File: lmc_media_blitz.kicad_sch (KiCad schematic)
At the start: 46 parts, among them J1 Conn_ARM_JTAG_SWD_10, Q1 BSS138, Q2 BSS138, U1 TPS61222DCK, U2 TLV77333PDBVR, U3 LPC804M101JDH20, U4 ST25R3918AQW, U5 SK9822, U6 SK9822, U7 SK9822, U8 SK9822, U9 SK9822, Y1 27.12MHz

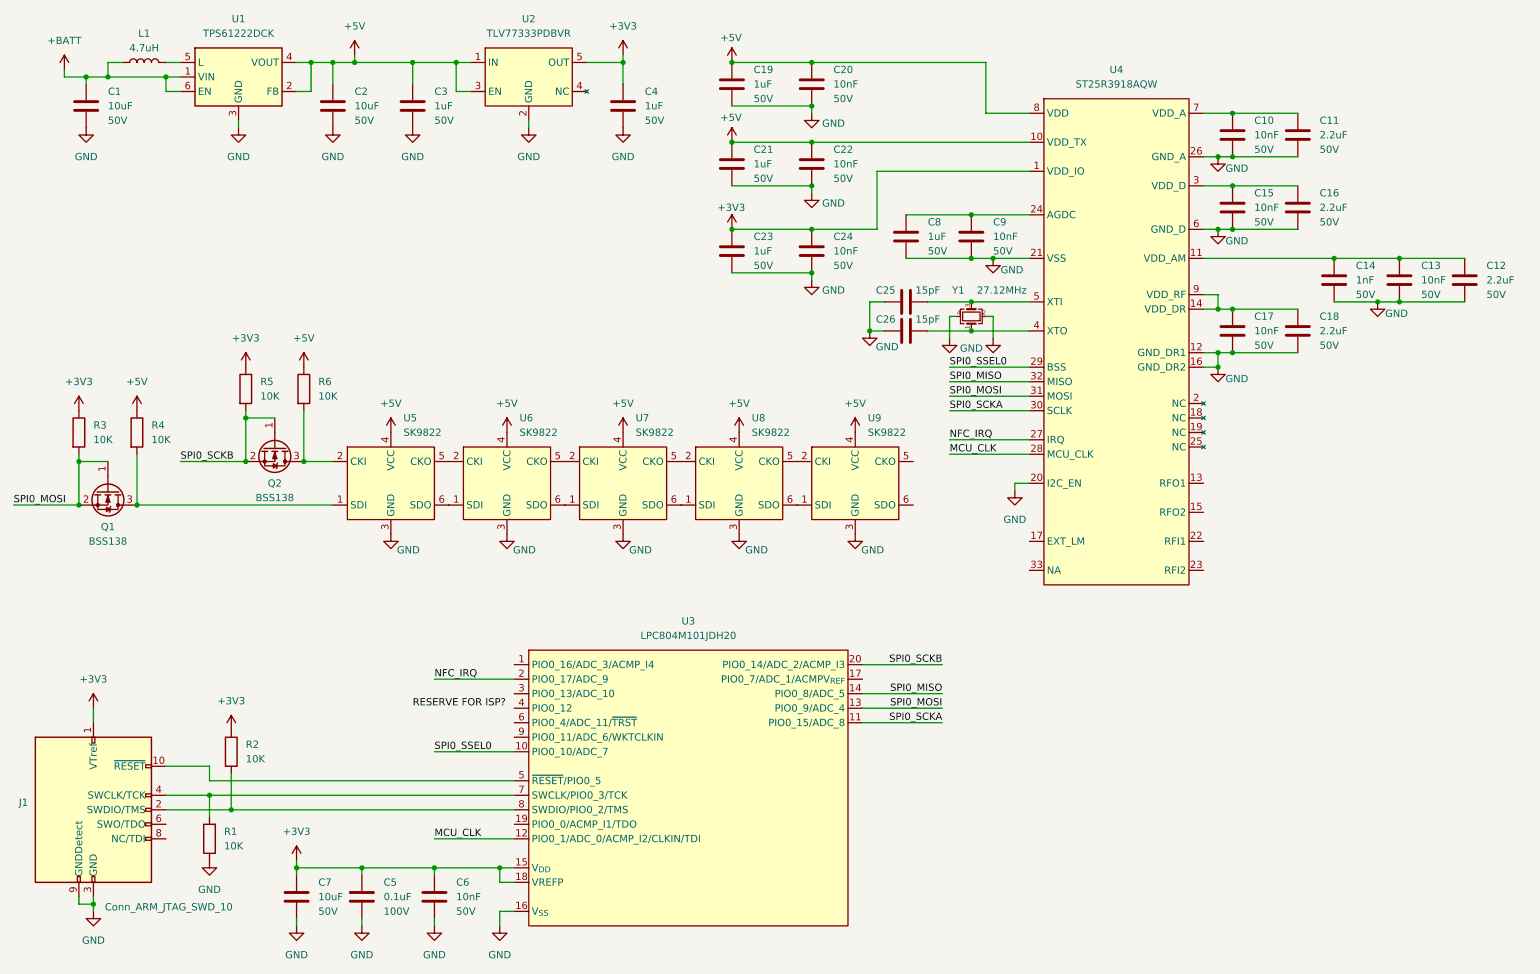
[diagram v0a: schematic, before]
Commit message: Added some footprints and cap touch symbols
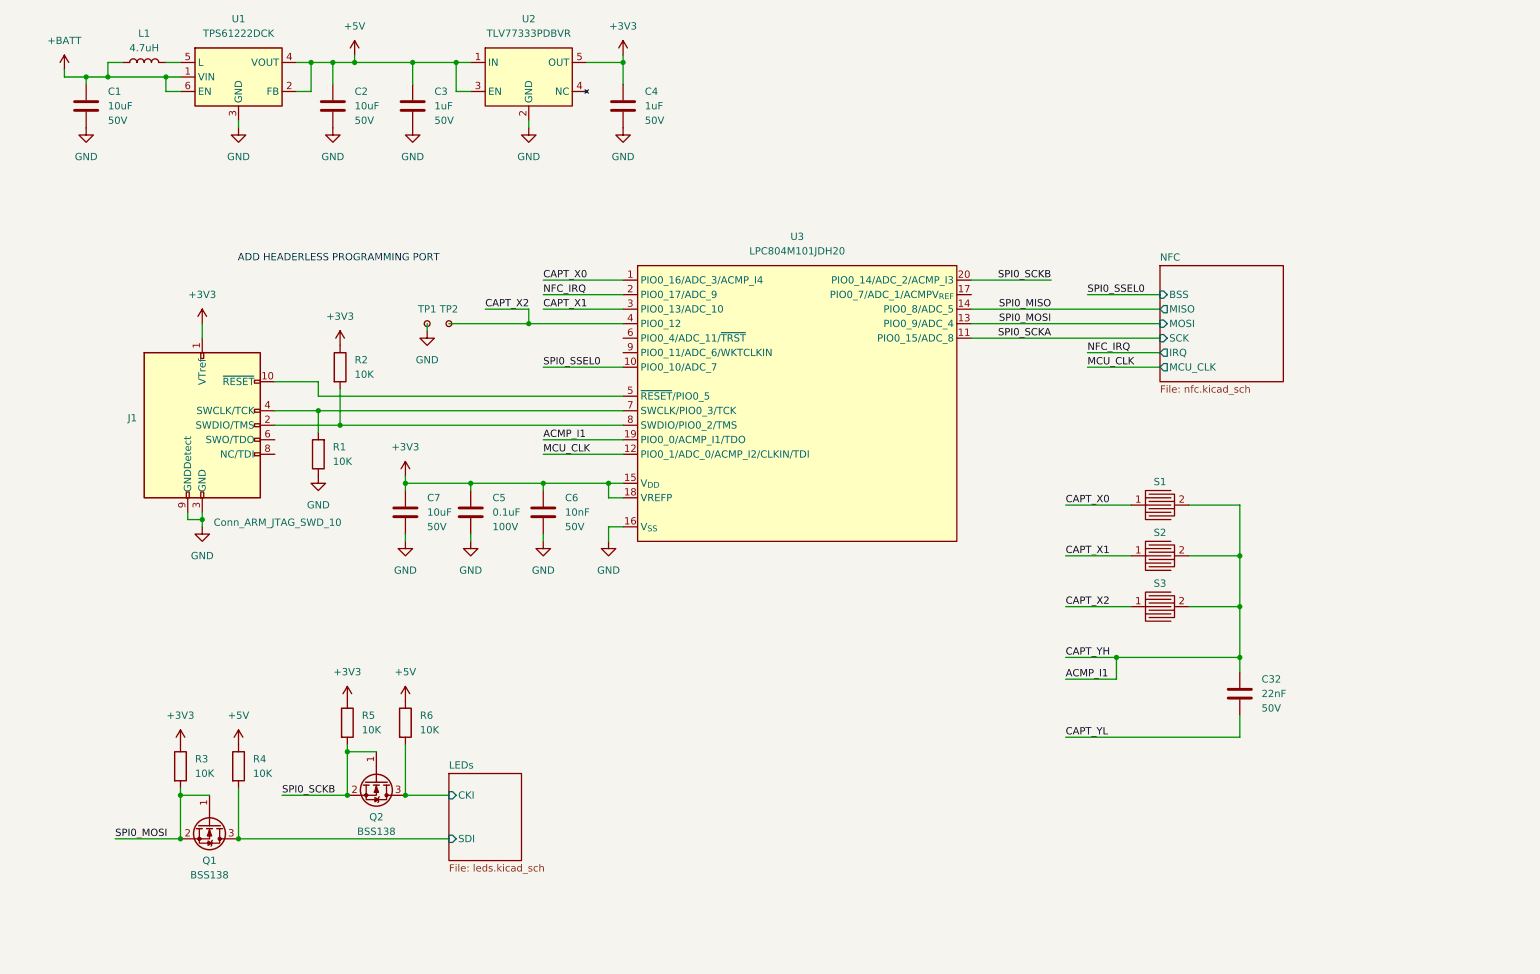
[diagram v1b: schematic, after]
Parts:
- removed C10, C13, C15, C17, C20, C22, C24, C9: 10nF, 0805, symbol Device:C
- removed C11, C12, C16, C18: 2.2uF, 0805, symbol Device:C
- removed C14: 1nF, 0805, symbol Device:C
- removed C19, C21, C23, C8: 1uF, 0805, symbol Device:C
- removed C25, C26: 15pF, 0603, symbol Device:C
- removed U4: ST25R3918AQW, VFQFPN32, symbol parts:ST25R3918AQW
- removed U5, U6, U7, U8, U9: SK9822, symbol parts:SK99822
- removed Y1: 27.12MHz, SMD3225-4P, symbol Device:Crystal_GND24_Small
- added C32: 22nF, 0805, symbol Device:C
- added S1, S2, S3: ~, symbol parts:CapTouchPad
- added TP1, TP2: TestPoint_Small, symbol Connector:TestPoint_Small
- C1, C2, C3, C4, C5, C6, C7: footprint 0805 -> Capacitor_SMD:C_0805_2012Metric
- J1: MFPN (none) -> FTSH-105-01-L-DV-007-K
- L1: footprint (none) -> Inductor_SMD:L_Taiyo-Yuden_MD-3030
- R1, R2, R3, R4, R5, R6: footprint 0805 -> Resistor_SMD:R_0805_2012Metric
- U2: footprint SOT23-5 -> Package_TO_SOT_SMD:SOT-23-5
- U3: footprint SOT360-1 -> Package_SO:TSSOP-20_4.4x6.5mm_P0.65mm
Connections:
- net GND: now also TP1.1
- net LEDs/SDI: now reaches Q1.3 (D), R4.2
- net LEDs/CKI: now reaches Q2.3 (D), R6.2
- net CAPT_X0: now reaches U3.1 (PIO0_16/ADC_3/ACMP_I4)
- net CAPT_X0: now also S1.1
- net ACMP_I1: now reaches U3.19 (PIO0_0/ACMP_I1/TDO)
- net ACMP_I1: now also C32.1, S1.2, S2.2, S3.2
- net CAPT_X1: now reaches U3.3 (PIO0_13/ADC_10)
- net CAPT_X1: now also S2.1
- net CAPT_X2: now reaches U3.4 (PIO0_12)
- net CAPT_X2: now also S3.1, TP2.1
- new net CAPT_YL: C32.2
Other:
- added sheet LEDs (leds.kicad_sch)
- added sheet NFC (nfc.kicad_sch)
- note added: "ADD HEADERLESS PROGRAMMING PORT"
- moved on the sheet: C5, C6, C7, J1, Q1, Q2, R1, R2, R3, R4, R5, R6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

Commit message: Adding some stuf
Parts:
- added J2, J3: ~, footprints:Keystone82, symbol parts:Keystone82
- C32: footprint 0805 -> Capacitor_SMD:C_0805_2012Metric
- J1: footprint (none) -> Capacitor_SMD:C_0805_2012Metric
- TP1, TP2: footprint (none) -> TestPoint:TestPoint_Pad_D2.0mm
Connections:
- net +BATT: now also J2.1, J2.2
- net ACMP_I1: now also U3.9 (PIO0_11/ADC_6/WKTCLKIN)
- net CAPT_YL: now also U3.6 (PIO0_4/ADC_11/~{TRST})
- net GND: now also J3.1, J3.2
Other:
- moved on the sheet: C1, C2, C3, C32, C4, C5, C6, C7, J1, L1, Q1, Q2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

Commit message: WIP
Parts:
- added TP3, TP4: TestPoint_Small, TestPoint:TestPoint_Pad_D2.0mm, symbol Connector:TestPoint_Small
- C5: footprint Capacitor_SMD:C_0805_2012Metric -> Capacitor_SMD:C_0603_1608Metric; MFPN CL21B104KCFNNNE -> CC0603KRX7R9BB104; Voltage 100V -> 50V
- C6: footprint Capacitor_SMD:C_0805_2012Metric -> Capacitor_SMD:C_0603_1608Metric; MFPN CL21B103KBANNNC -> CC0603KRX7R9BB103
- renumbered J2 to J1, J3 to J2, J1 to J3
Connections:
- net +3V3: now also TP4.1
- net +5V: now also TP3.1
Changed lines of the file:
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@@
 	)
 	(junction
+		(at 125.73 27.94)
+		(diameter 0)
+		(color 0 0 0 0)
+	)
+	(junction
 		(at 226.06 140.97)
 		(diameter 0)
@@
 	)
 	(junction
+		(at 88.9 27.94)
+		(diameter 0)
+		(color 0 0 0 0)
+	)
+	(junction
 		(at 204.47 140.97)
 		(diameter 0)
@@
 	(wire
 		(pts
-			(xy 124.46 27.94) (xy 130.81 27.94)
+			(xy 124.46 27.94) (xy 125.73 27.94)
 		)
 		(stroke
@@
 	(wire
 		(pts
+			(xy 88.9 25.4) (xy 88.9 27.94)
+		)
+		(stroke
+			(width 0)
+			(type default)
+		)
+	)
+	(wire
+		(pts
 			(xy 115.57 113.03) (xy 115.57 110.49)
 		)
@@
 	(wire
 		(pts
+			(xy 88.9 27.94) (xy 93.98 27.94)
+		)
+		(stroke
+			(width 0)
+			(type default)
+		)
+	)
+	(wire
+		(pts
 			(xy 199.39 87.63) (xy 212.09 87.63)
 		)
@@
 	(wire
 		(pts
+			(xy 125.73 27.94) (xy 130.81 27.94)
+		)
+		(stroke
+			(width 0)
+			(type default)
+		)
+	)
+	(wire
+		(pts
 			(xy 33.02 30.48) (xy 33.02 29.21)
 		)
@@
 	(wire
 		(pts
+			(xy 125.73 25.4) (xy 125.73 27.94)
+		)
+		(stroke
+			(width 0)
+			(type default)
+		)
+	)
+	(wire
+		(pts
 			(xy 195.58 144.78) (xy 204.47 144.78)
 		)
@@
 	(wire
 		(pts
-			(xy 83.82 27.94) (xy 93.98 27.94)
+			(xy 83.82 27.94) (xy 88.9 27.94)
 		)
 		(stroke
@@
 		(on_board yes)
 		(dnp no)
-		(property "Reference" "J3"
+		(property "Reference" "J2"
 			(at 22.606 49.53 0)
 			(effects
@@
 			(project "lmc_media_blitz"
 				(path "/b87eb037-3127-4116-a225-5eb939725614"
-					(reference "J3")
+					(reference "J2")
 					(unit 1)
 				)
@@
 	)
 	(symbol
+		(lib_id "Connector:TestPoint_Small")
+		(at 88.9 25.4 90)
+		(unit 1)
+		(exclude_from_sim no)
+		(in_bom yes)
+		(on_board yes)
+		(dnp no)
+		(fields_autoplaced yes)
+		(property "Reference" "TP3"
+			(at 88.9 22.86 90)
+			(effects
+				(font
+					(size 1.27 1.27)
+				)
+			)
+		)
+		(property "Value" "TestPoint_Small"
+			(at 90.1699 24.13 0)
+			(effects
+				(font
+					(size 1.27 1.27)
+				)
+				(justify left)
+				(hide yes)
+			)
+		)
+		(property "Footprint" "TestPoint:TestPoint_Pad_D2.0mm"
+			(at 88.9 20.32 0)
+			(effects
+				(font
+					(size 1.27 1.27)
+				)
+				(hide yes)
+			)
+		)
+		(property "Datasheet" "~"
+			(at 88.9 20.32 0)
+			(effects
+				(font
+					(size 1.27 1.27)
+				)
+				(hide yes)
+			)
+		)
+		(property "Description" "test point"
+			(at 88.9 25.4 0)
+			(effects
+				(font
+					(size 1.27 1.27)
+				)
+				(hide yes)
+			)
+		)
+		(pin "1"
+		)
+		(instances
+			(project "lmc_media_blitz"
+				(path "/b87eb037-3127-4116-a225-5eb939725614"
+					(reference "TP3")
+					(unit 1)
+				)
+			)
+		)
+	)
+	(symbol
 		(lib_id "Device:C")
 		(at 36.83 35.56 180)
@@
 		(on_board yes)
 		(dnp no)
-		(property "Reference" "J1"
+		(property "Reference" "J3"
 			(at 33.02 99.0599 0)
 			(effects
@@
 			(project ""
 				(path "/b87eb037-3127-4116-a225-5eb939725614"
-					(reference "J1")
+					(reference "J3")
 					(unit 1)
 				)
@@
 		(dnp no)
 		(fields_autoplaced yes)
-		(property "Reference" "J2"
+		(property "Reference" "J1"
 			(at 22.606 21.59 0)
 			(effects
@@
 			(project ""
 				(path "/b87eb037-3127-4116-a225-5eb939725614"
-					(reference "J2")
+					(reference "J1")
 					(unit 1)
 				)
@@
 	)
 	(symbol
+		(lib_id "Device:C")
+		(at 104.14 115.57 0)
+		(unit 1)
+		(exclude_from_sim no)
+		(in_bom yes)
+		(on_board yes)
+		(dnp no)
+		(fields_autoplaced yes)
+		(property "Reference" "C6"
+			(at 107.95 113.0299 0)
+			(effects
+				(font
+					(size 1.27 1.27)
+				)
+				(justify left)
+			)
+		)
+		(property "Value" "10nF"
+			(at 107.95 115.5699 0)
+			(effects
+				(font
+					(size 1.27 1.27)
+				)
+				(justify left)
+			)
+		)
+		(property "Footprint" "Capacitor_SMD:C_0603_1608Metric"
+			(at 105.1052 119.38 0)
+			(effects
+				(font
+					(size 1.27 1.27)
+				)
+				(hide yes)
+			)
+		)
+		(property "Datasheet" "~"
+			(at 104.14 115.57 0)
+			(effects
+				(font
+					(size 1.27 1.27)
+				)
+				(hide yes)
+			)
+		)
+		(property "Description" "Unpolarized capacitor"
+			(at 104.14 115.57 0)
+			(effects
+				(font
+					(size 1.27 1.27)
+				)
+				(hide yes)
+			)
+		)
+		(property "MFPN" "CC0603KRX7R9BB103"
+			(at 104.14 115.57 0)
+			(effects
+				(font
+					(size 1.27 1.27)
+				)
+				(hide yes)
+			)
+		)
+		(property "Voltage" "50V"
+			(at 107.95 118.1099 0)
+			(effects
+				(font
+					(size 1.27 1.27)
+				)
+				(justify left)
+			)
+		)
+		(pin "1"
+		)
+		(pin "2"
+		)
+		(instances
+			(project "lmc_media_blitz"
+				(path "/b87eb037-3127-4116-a225-5eb939725614"
+					(reference "C6")
+					(unit 1)
+				)
+			)
+		)
+	)
+	(symbol
 		(lib_id "power:+BATT")
 		(at 33.02 29.21 0)
@@
 			)
 		)
-		(property "Footprint" "Capacitor_SMD:C_0805_2012Metric"
+		(property "Footprint" "Capacitor_SMD:C_0603_1608Metric"
 			(at 92.4052 119.38 0)
 			(effects
@@
 			)
 		)
-		(property "MFPN" "CL21B104KCFNNNE"
+		(property "MFPN" "CC0603KRX7R9BB104"
 			(at 91.44 115.57 0)
 			(effects
@@
 			)
 		)
-		(property "Voltage" "100V"
+		(property "Voltage" "50V"
 			(at 95.25 118.1099 0)
 			(effects
@@
 	)
 	(symbol
-		(lib_id "Device:C")
-		(at 104.14 115.57 0)
-		(unit 1)
-		(exclude_from_sim no)
-		(in_bom yes)
-		(on_board yes)
-		(dnp no)
-		(fields_autoplaced yes)
-		(property "Reference" "C6"
-			(at 107.95 113.0299 0)
-			(effects
-				(font
-					(size 1.27 1.27)
-				)
-				(justify left)
-			)
-		)
-		(property "Value" "10nF"
-			(at 107.95 115.5699 0)
-			(effects
-				(font
-					(size 1.27 1.27)
-				)
-				(justify left)
-			)
-		)
-		(property "Footprint" "Capacitor_SMD:C_0805_2012Metric"
-			(at 105.1052 119.38 0)
-			(effects
-				(font
-					(size 1.27 1.27)
-				)
-				(hide yes)
-			)
-		)
-		(property "Datasheet" "~"
-			(at 104.14 115.57 0)
-			(effects
-				(font
-					(size 1.27 1.27)
-				)
-				(hide yes)
-			)
-		)
-		(property "Description" "Unpolarized capacitor"
-			(at 104.14 115.57 0)
-			(effects
-				(font
-					(size 1.27 1.27)
-				)
-				(hide yes)
-			)
-		)
-		(property "MFPN" "CL21B103KBANNNC"
-			(at 104.14 115.57 0)
-			(effects
-				(font
-					(size 1.27 1.27)
-				)
-				(hide yes)
-			)
-		)
-		(property "Voltage" "50V"
-			(at 107.95 118.1099 0)
-			(effects
-				(font
-					(size 1.27 1.27)
-				)
-				(justify left)
-			)
-		)
-		(pin "1"
-		)
-		(pin "2"
-		)
-		(instances
-			(project "lmc_media_blitz"
-				(path "/b87eb037-3127-4116-a225-5eb939725614"
-					(reference "C6")
-					(unit 1)
-				)
-			)
-		)
-	)
-	(symbol
 		(lib_id "power:+5V")
 		(at 218.44 43.18 0)
@@
 					(unit 1)
 				)
+			)
+		)
+	)
+	(symbol
+		(lib_id "Connector:TestPoint_Small")
+		(at 125.73 25.4 90)
+		(unit 1)
+		(exclude_from_sim no)
+		(in_bom yes)
+		(on_board yes)
+		(dnp no)
+		(fields_autoplaced yes)
+		(property "Reference" "TP4"
+			(at 125.73 22.86 90)
+			(effects
+				(font
+					(size 1.27 1.27)
+				)
+			)
+		)
+		(property "Value" "TestPoint_Small"
+			(at 126.9999 24.13 0)
+			(effects
+				(font
+					(size 1.27 1.27)
+				)
+				(justify left)
+				(hide yes)
+			)
+		)
+		(property "Footprint" "TestPoint:TestPoint_Pad_D2.0mm"
+			(at 125.73 20.32 0)
+			(effects
+				(font
+					(size 1.27 1.27)
+				)
+				(hide yes)
+			)
+		)
+		(property "Datasheet" "~"
+			(at 125.73 20.32 0)
+			(effects
+				(font
+					(size 1.27 1.27)
+				)
+				(hide yes)
+			)
+		)
+		(property "Description" "test point"
+			(at 125.73 25.4 0)
+			(effects
+				(font
+					(size 1.27 1.27)
+				)
+				(hide yes)
+			)
+		)
+		(pin "1"
+		)
+		(instances
+			(project "lmc_media_blitz"
+				(path "/b87eb037-3127-4116-a225-5eb939725614"
+					(reference "TP4")
+					(unit 1)
+				)

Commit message: WIP
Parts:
- J3: footprint Capacitor_SMD:C_0805_2012Metric -> Connector_PinHeader_1.27mm:PinHeader_2x05_P1.27mm_Vertical_SMD
- S1, S2, S3: footprint (none) -> footprints:CapTouchButton
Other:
- moved on the sheet: TP1
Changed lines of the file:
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@@
 	(wire
 		(pts
-			(xy 83.82 82.55) (xy 83.82 83.82)
+			(xy 48.26 39.37) (xy 48.26 40.64)
 		)
 		(stroke
@@
 	(symbol
 		(lib_id "Connector:TestPoint_Small")
-		(at 83.82 82.55 90)
+		(at 48.26 39.37 90)
 		(unit 1)
 		(exclude_from_sim no)
@@
 		(fields_autoplaced yes)
 		(property "Reference" "TP1"
-			(at 83.82 80.01 90)
+			(at 48.26 36.83 90)
 			(effects
 				(font
@@
 		)
 		(property "Value" "TestPoint_Small"
-			(at 85.0899 81.28 0)
+			(at 49.5299 38.1 0)
 			(effects
 				(font
@@
 		)
 		(property "Footprint" "TestPoint:TestPoint_Pad_D2.0mm"
-			(at 83.82 77.47 0)
+			(at 48.26 34.29 0)
 			(effects
 				(font
@@
 		)
 		(property "Datasheet" "~"
-			(at 83.82 77.47 0)
+			(at 48.26 34.29 0)
 			(effects
 				(font
@@
 		)
 		(property "Description" "test point"
-			(at 83.82 82.55 0)
+			(at 48.26 39.37 0)
 			(effects
 				(font
@@
 			)
 		)
-		(property "Footprint" "Capacitor_SMD:C_0805_2012Metric"
+		(property "Footprint" "Connector_PinHeader_1.27mm:PinHeader_2x05_P1.27mm_Vertical_SMD"
 			(at 44.45 100.33 0)
 			(effects
@@
 			)
 		)
-		(property "Footprint" ""
+		(property "Footprint" "footprints:CapTouchButton"
 			(at 212.09 132.08 0)
 			(effects
@@
 			)
 		)
-		(property "Footprint" ""
+		(property "Footprint" "footprints:CapTouchButton"
 			(at 212.09 123.19 0)
 			(effects
@@
 			)
 		)
-		(property "Footprint" ""
+		(property "Footprint" "footprints:CapTouchButton"
 			(at 212.09 114.3 0)
 			(effects
@@
 	(symbol
 		(lib_id "power:GND")
-		(at 83.82 83.82 0)
+		(at 48.26 40.64 0)
 		(unit 1)
 		(exclude_from_sim no)
@@
 		(fields_autoplaced yes)
 		(property "Reference" "#PWR048"
-			(at 83.82 90.17 0)
+			(at 48.26 46.99 0)
 			(effects
 				(font
@@
 		)
 		(property "Value" "GND"
-			(at 83.82 88.9 0)
+			(at 48.26 45.72 0)
 			(effects
 				(font
@@
 		)
 		(property "Footprint" ""
-			(at 83.82 83.82 0)
+			(at 48.26 40.64 0)
 			(effects
 				(font
@@
 		)
 		(property "Datasheet" ""
-			(at 83.82 83.82 0)
+			(at 48.26 40.64 0)
 			(effects
 				(font
@@
 		)
 		(property "Description" "Power symbol creates a global label with name \"GND\" , ground"
-			(at 83.82 83.82 0)
+			(at 48.26 40.64 0)
 			(effects
 				(font

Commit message: Initial routing
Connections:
- net CAPT_X0: now also U3.3 (PIO0_13/ADC_10); no longer U3.1 (PIO0_16/ADC_3/ACMP_I4)
- net CAPT_X1: now also TP2.1, U3.4 (PIO0_12); no longer U3.3 (PIO0_13/ADC_10)
- net CAPT_X2: now also U3.6 (PIO0_4/ADC_11/~{TRST}); no longer TP2.1, U3.4 (PIO0_12)
- net CAPT_YL: now also U3.19 (PIO0_0/ACMP_I1/TDO); no longer U3.6 (PIO0_4/ADC_11/~{TRST})
- net NFC_IRQ: now also U3.9 (PIO0_11/ADC_6/WKTCLKIN); no longer U3.2 (PIO0_17/ADC_9)
- net ACMP_I1 renamed ACMP_I4
- net ACMP_I4: now also U3.1 (PIO0_16/ADC_3/ACMP_I4), U3.2 (PIO0_17/ADC_9); no longer U3.19 (PIO0_0/ACMP_I1/TDO), U3.9 (PIO0_11/ADC_6/WKTCLKIN)
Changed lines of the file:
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@@
+		)
+	)
+	(label "CAPT_X1"
+		(at 93.98 80.01 0)
+		(effects
+			(font
+				(size 1.27 1.27)
+			)
+			(justify left bottom)
 		)
 	)
@@
 		)
 	)
-	(label "CAPT_YH"
-		(at 104.14 87.63 0)
-		(effects
-			(font
-				(size 1.27 1.27)
-			)
-			(justify left bottom)
-		)
-	)
 	(label "CAPT_YL"
 		(at 195.58 154.94 0)
@@
 		)
 	)
+	(label "CAPT_YH"
+		(at 104.14 77.47 0)
+		(effects
+			(font
+				(size 1.27 1.27)
+			)
+			(justify left bottom)
+		)
+	)
 	(label "SPI0_MOSI"
 		(at 193.04 82.55 180)
@@
 		)
 	)
-	(label "CAPT_X1"
-		(at 104.14 80.01 0)
-		(effects
-			(font
-				(size 1.27 1.27)
-			)
-			(justify left bottom)
-		)
-	)
 	(label "NFC_IRQ"
 		(at 199.39 87.63 0)
@@
 		)
 	)
-	(label "CAPT_X2"
-		(at 93.98 80.01 0)
+	(label "CAPT_YL"
+		(at 104.14 102.87 0)
 		(effects
 			(font
@@
 		)
 	)
-	(label "CAPT_YL"
-		(at 104.14 85.09 0)
-		(effects
-			(font
-				(size 1.27 1.27)
-			)
-			(justify left bottom)
-		)
-	)
 	(label "SPI0_SCKA"
 		(at 193.04 85.09 180)
@@
 		)
 	)
-	(label "ACMP_I1"
+	(label "ACMP_I4"
 		(at 195.58 144.78 0)
+		(effects
+			(font
+				(size 1.27 1.27)
+			)
+			(justify left bottom)
+		)
+	)
+	(label "CAPT_X2"
+		(at 104.14 85.09 0)
+		(effects
+			(font
+				(size 1.27 1.27)
+			)
+			(justify left bottom)
+		)
+	)
+	(label "ACMP_I4"
+		(at 104.14 74.93 0)
+		(effects
+			(font
+				(size 1.27 1.27)
+			)
+			(justify left bottom)
+		)
+	)
+	(label "CAPT_X0"
+		(at 104.14 80.01 0)
 		(effects
 			(font
@@
 		)
 	)
-	(label "NFC_IRQ"
-		(at 104.14 77.47 0)
-		(effects
-			(font
-				(size 1.27 1.27)
-			)
-			(justify left bottom)
-		)
-	)
 	(label "MCU_CLK"
 		(at 199.39 90.17 0)
@@
 		)
 	)
-	(label "ACMP_I1"
-		(at 104.14 102.87 0)
+	(label "NFC_IRQ"
+		(at 104.14 87.63 0)
 		(effects
 			(font
@@
 		(effects
 			(font
-				(size 1.27 1.27)
-			)
-			(justify left bottom)
-		)
-	)
-	(label "CAPT_X0"
-		(at 104.14 74.93 0)
-		(effects
-			(font
